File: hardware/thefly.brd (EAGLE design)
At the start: 54 x 54 mm, 37 parts, among them IC1 AP7313-1.8, J1 54-00298-HOLES, U1 SGTL5000XNLA3, U2 MAX4466EXK

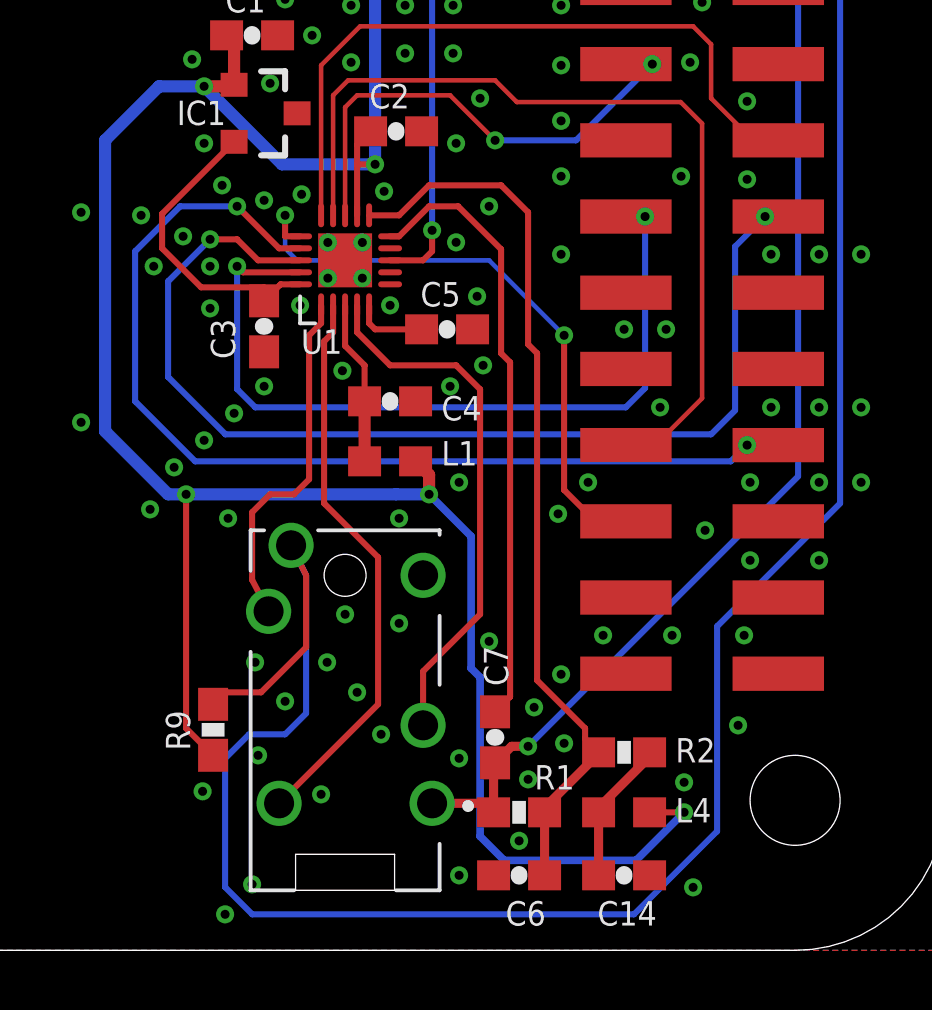
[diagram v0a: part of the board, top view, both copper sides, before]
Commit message: pcb layout changes, removed L4, added comments
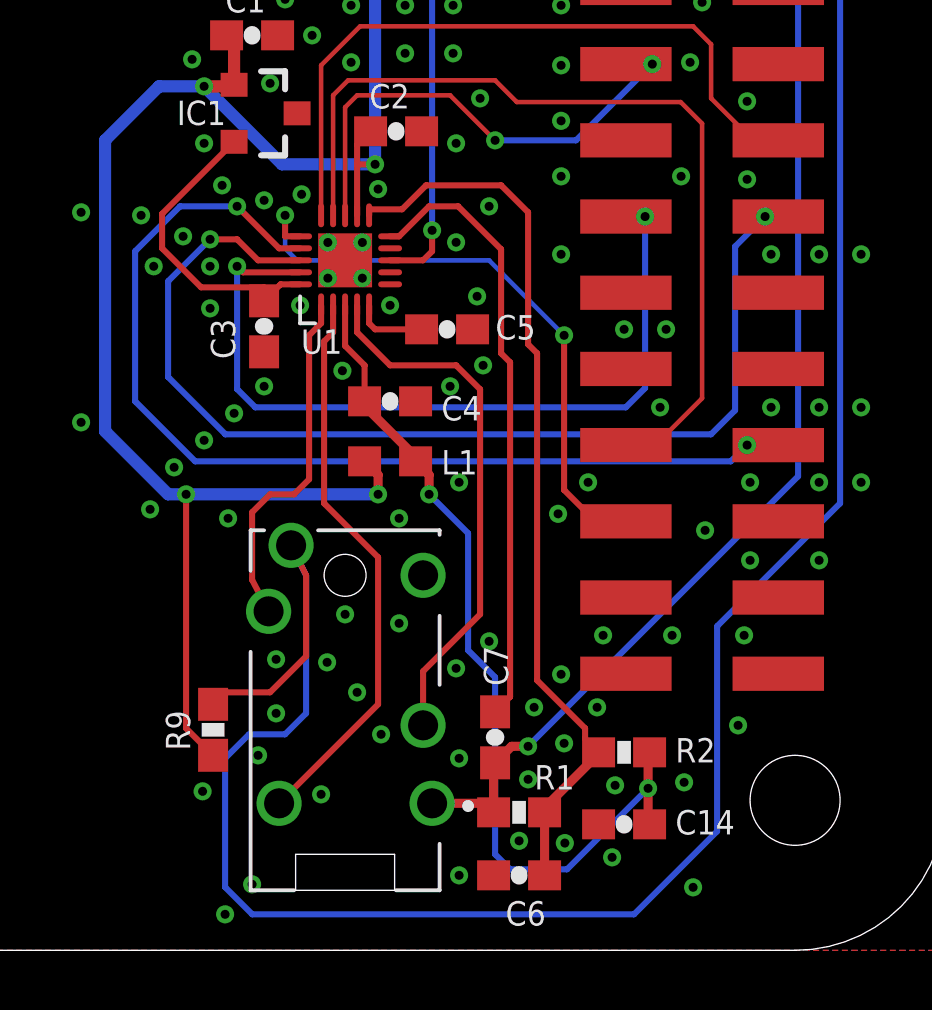
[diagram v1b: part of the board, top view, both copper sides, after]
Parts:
- removed L4: 600, thefly:0603
- moved C14 1.70 mm to (43.3, 4.20), turned to 180 degrees
- turned L1 to 180 degrees
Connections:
- removed net N$1: C14.1, L4.2, R2.1
- net 3.3V: no longer L4.1
- net VDDA: now also C14.1, R2.1
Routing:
- net VDDA: track 5.47 -> 29.4 mm, vias 0 -> 2
- net 3.3V: track 88.5 -> 65.2 mm, vias 6 -> 5
- net N$1: track 4.80 -> 0.00 mm
- net GND: vias 110 -> 115

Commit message: pcb layout use ledc pwm mclk
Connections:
- net MCLK: now also JP1.16; no longer JP1.14
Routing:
- net MCLK: track 16.6 -> 13.7 mm, vias 2 -> 0
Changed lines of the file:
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@@
 <wire x1="34.4" y1="28.5" x2="37.5" y2="28.5" width="0.1524" layer="1"/>
 <wire x1="37.5" y1="28.5" x2="39" y2="27" width="0.1524" layer="1"/>
-<via x="39" y="27" extent="1-16" drill="0.3" shape="octagon"/>
-<wire x1="39" y1="27" x2="41.7" y2="27" width="0.2032" layer="16"/>
-<wire x1="41.7" y1="27" x2="44.24" y2="29.54" width="0.2032" layer="16"/>
-<via x="44.24" y="29.54" extent="1-16" drill="0.3" shape="octagon"/>
-<contactref element="JP1" pad="14"/>
-<wire x1="44.24" y1="29.54" x2="43.36" y2="29.54" width="0.2032" layer="1"/>
+<contactref element="JP1" pad="16"/>
+<wire x1="39" y1="27" x2="39.3" y2="27" width="0.1524" layer="1"/>
+<wire x1="39.3" y1="27" x2="39.6" y2="27" width="0.17" layer="1"/>
+<wire x1="39.6" y1="27" x2="43.36" y2="27" width="0.2" layer="1"/>
 </signal>
 <signal name="VCCA2">

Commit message: layout change to add dc block on mic path
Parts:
- added C15: 100n, thefly:0603-CAP
- moved C14 33.8 mm to (32.8, 36.3), turned to 270 degrees
- moved L3 2.00 mm to (30.0, 33.8)
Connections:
- new net ASDASDASD: C10.2, C14.1, R7.1, U2.4
- net GND: now also C15.2; no longer C14.2
- net MIC2: now also C14.2; no longer C10.2, R7.1, U2.4
- net VDDA: now also C15.1; no longer C14.1
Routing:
- net ASDASDASD: track 0.00 -> 5.31 mm
- net MIC2: track 23.6 -> 19.4 mm
- net GND: vias 115 -> 114
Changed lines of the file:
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@@
 </element>
 <element name="L2" library="thefly" package="0603" value="600" x="35" y="36.2" smashed="yes" rot="R90">
-<attribute name="NAME" x="34.238" y="34.311" size="0.8128" layer="25" font="vector" rot="R90"/>
+<attribute name="NAME" x="34.862" y="34.789" size="0.8128" layer="25" font="vector" rot="R270"/>
 <attribute name="VALUE" x="36.143" y="35.184" size="0.8128" layer="27" font="vector" rot="R90"/>
 </element>
-<element name="L3" library="thefly" package="0603" value="600" x="32" y="33.8" smashed="yes" rot="R90">
-<attribute name="NAME" x="31.238" y="32.911" size="0.8128" layer="25" font="vector" rot="R90"/>
-<attribute name="VALUE" x="33.143" y="32.784" size="0.8128" layer="27" font="vector" rot="R90"/>
+<element name="L3" library="thefly" package="0603" value="600" x="30" y="33.8" smashed="yes" rot="R90">
+<attribute name="NAME" x="29.238" y="32.911" size="0.8128" layer="25" font="vector" rot="R90"/>
+<attribute name="VALUE" x="31.143" y="32.784" size="0.8128" layer="27" font="vector" rot="R90"/>
 </element>
 <element name="R3" library="thefly" package="0603-RES" value="1K" x="38.2" y="44.9" smashed="yes" rot="R180">
@@
 </element>
 <element name="R7" library="thefly" package="0603-RES" value="100K" x="31.9" y="39.7" smashed="yes" rot="R90">
-<attribute name="NAME" x="31.362" y="38.189" size="0.8128" layer="25" font="vector" rot="R270"/>
+<attribute name="NAME" x="30.762" y="38.689" size="0.8128" layer="25" font="vector" rot="R270"/>
 <attribute name="VALUE" x="33.043" y="38.684" size="0.8128" layer="27" font="vector" rot="R90"/>
 </element>
@@
 <attribute name="VALUE" x="30.143" y="46.384" size="0.4064" layer="27" font="vector" rot="R90"/>
 </element>
-<element name="C14" library="thefly" package="0603-CAP" value="100n" x="43.3" y="4.2" smashed="yes" rot="R180">
+<element name="C15" library="thefly" package="0603-CAP" value="100n" x="43.3" y="4.2" smashed="yes" rot="R180">
 <attribute name="NAME" x="45.011" y="3.862" size="0.8128" layer="25" font="vector"/>
 <attribute name="VALUE" x="44.316" y="5.343" size="0.4064" layer="27" font="vector" rot="R180"/>
 </element>
 <element name="U$5" library="thefly" package="THE-FLY-LOGO" value="THE-FLY-LOGO" x="18" y="51"/>
+<element name="C14" library="thefly" package="0603-CAP" value="100n" x="32.8" y="36.3" smashed="yes" rot="R270">
+<attribute name="NAME" x="32.362" y="34.789" size="0.8128" layer="25" font="vector" rot="R270"/>
+<attribute name="VALUE" x="31.657" y="37.316" size="0.4064" layer="27" font="vector" rot="R270"/>
+</element>
 </elements>
 <signals>
@@
 <wire x1="34.65" y1="19.5" x2="34.65" y2="18.3" width="0.2032" layer="1"/>
 <contactref element="R2" pad="1"/>
-<contactref element="C14" pad="1"/>
+<contactref element="C15" pad="1"/>
 <wire x1="44.15" y1="6.45" x2="44.15" y2="6.6" width="0.3048" layer="1"/>
 <via x="36.8" y="15.2" extent="1-16" drill="0.3" shape="octagon"/>
@@
 <via x="51.2" y="41" extent="1-16" drill="0.3" shape="octagon"/>
 <via x="51.2" y="38.4" extent="1-16" drill="0.3" shape="octagon"/>
-<contactref element="C14" pad="2"/>
+<contactref element="C15" pad="2"/>
 <via x="45.6" y="2.1" extent="1-16" drill="0.3" shape="octagon"/>
 <via x="45.3" y="5.6" extent="1-16" drill="0.3" shape="octagon"/>
@@
 <via x="31.1" y="6.5" extent="1-16" drill="0.3" shape="octagon"/>
 <via x="37.8" y="6.4" extent="1-16" drill="0.3" shape="octagon"/>
-<via x="34.4" y="8.6" extent="1-16" drill="0.3" shape="octagon"/>
 <via x="35.2" y="7.2" extent="1-16" drill="0.3" shape="octagon"/>
 <via x="33.2" y="5.2" extent="1-16" drill="0.3" shape="octagon"/>
@@
 <wire x1="33.3" y1="20.3" x2="33.3" y2="14.9" width="0.2032" layer="1"/>
 <wire x1="33.3" y1="14.9" x2="35.1" y2="13.1" width="0.2032" layer="1"/>
-<wire x1="35.1" y1="13.1" x2="35.1" y2="8.2" width="0.2032" layer="1"/>
-<wire x1="35.1" y1="8.2" x2="31.8" y2="4.9" width="0.2032" layer="1"/>
+<wire x1="35.1" y1="13.1" x2="35.1" y2="9.6" width="0.2032" layer="1"/>
+<wire x1="35.1" y1="9.6" x2="31.8" y2="6.3" width="0.2032" layer="1"/>
+<wire x1="31.8" y1="6.3" x2="31.8" y2="4.9" width="0.2032" layer="1"/>
 </signal>
 <signal name="HP-SENSE-L">
@@
 </signal>
 <signal name="MIC2">
-<contactref element="U2" pad="4"/>
-<contactref element="R7" pad="1"/>
-<contactref element="C10" pad="2"/>
 <contactref element="U1" pad="8"/>
-<wire x1="33.35" y1="38.74" x2="32.01" y2="38.74" width="0.3048" layer="1"/>
-<wire x1="32.01" y1="38.74" x2="31.9" y2="38.85" width="0.2032" layer="1"/>
-<wire x1="31.9" y1="38.85" x2="29.9" y2="38.85" width="0.3048" layer="1"/>
 <via x="36.9" y="24" extent="1-16" drill="0.3" shape="octagon"/>
 <wire x1="35.5" y1="23" x2="36.6" y2="23" width="0.2032" layer="1"/>
@@
 <wire x1="36.9" y1="24" x2="36.9" y2="34.487690625" width="0.2032" layer="16"/>
 <wire x1="36.9" y1="34.487690625" x2="36.487690625" y2="34.9" width="0.2032" layer="16"/>
-<wire x1="36.487690625" y1="34.9" x2="33.7" y2="34.9" width="0.2032" layer="16"/>
-<wire x1="33.7" y1="34.9" x2="33.3" y2="35.3" width="0.2032" layer="16"/>
-<wire x1="33.3" y1="35.3" x2="33.3" y2="37.3" width="0.2032" layer="16"/>
-<via x="33.3" y="37.3" extent="1-16" drill="0.3" shape="octagon"/>
-<wire x1="33.3" y1="37.3" x2="33.3" y2="38.74" width="0.3048" layer="1"/>
-<wire x1="33.3" y1="38.74" x2="33.35" y2="38.74" width="0.2032" layer="1"/>
+<wire x1="36.487690625" y1="34.9" x2="31.7" y2="34.9" width="0.2032" layer="16"/>
+<contactref element="C14" pad="2"/>
+<via x="31.7" y="34.9" extent="1-16" drill="0.3" shape="octagon"/>
+<wire x1="31.7" y1="34.9" x2="32.25" y2="34.9" width="0.2032" layer="1"/>
+<wire x1="32.25" y1="34.9" x2="32.8" y2="35.45" width="0.2032" layer="1"/>
 </signal>
 <signal name="N$6">
@@
 <via x="34" y="41.9" extent="1-16" drill="0.3" shape="octagon"/>
 <via x="33.95" y="36.7" extent="1-16" drill="0.3" shape="octagon"/>
-<via x="34" y="37.9" extent="1-16" drill="0.3" shape="octagon"/>
-<via x="32.4" y="37.7" extent="1-16" drill="0.3" shape="octagon"/>
+<via x="33.975" y="37.9" extent="1-16" drill="0.3" shape="octagon"/>
 <via x="32.7" y="43.6" extent="1-16" drill="0.3" shape="octagon"/>
 <via x="30.9" y="45.7" extent="1-16" drill="0.3" shape="octagon"/>
@@
 <via x="30.9" y="41.5" extent="1-16" drill="0.3" shape="octagon"/>
 <via x="32.7" y="41.6" extent="1-16" drill="0.3" shape="octagon"/>
-<via x="32" y="35.9" extent="1-16" drill="0.3" shape="octagon"/>
-<via x="30.8" y="34.7" extent="1-16" drill="0.3" shape="octagon"/>
 <via x="28.3" y="34.4" extent="1-16" drill="0.3" shape="octagon"/>
 <via x="28.3" y="53.4" extent="1-16" drill="0.3" shape="octagon"/>
@@
 <via x="36.1" y="47.8" extent="1-16" drill="0.3" shape="octagon"/>
 <via x="34.2" y="46" extent="1-16" drill="0.3" shape="octagon"/>
+<via x="31.1" y="34.3" extent="1-16" drill="0.3" shape="octagon"/>
+<via x="31.7" y="35.8" extent="1-16" drill="0.3" shape="octagon"/>
+<via x="31.7" y="37.7" extent="1-16" drill="0.3" shape="octagon"/>
 </signal>
 <signal name="N$9">
@@
 <wire x1="34" y1="47" x2="39.05" y2="47" width="0.3048" layer="16"/>
 </signal>
+<signal name="ASDASDASD">
+<contactref element="U2" pad="4"/>
+<contactref element="R7" pad="1"/>
+<contactref element="C10" pad="2"/>
+<contactref element="C14" pad="1"/>
+<wire x1="33.35" y1="38.74" x2="32.01" y2="38.74" width="0.3048" layer="1"/>
+<wire x1="32.01" y1="38.74" x2="31.9" y2="38.85" width="0.2032" layer="1"/>
+<wire x1="31.9" y1="38.85" x2="29.9" y2="38.85" width="0.3048" layer="1"/>
+<wire x1="32.8" y1="37.15" x2="33.35" y2="37.7" width="0.2032" layer="1"/>
+<wire x1="33.35" y1="37.7" x2="33.35" y2="38.74" width="0.2032" layer="1"/>
+</signal>
 </signals>

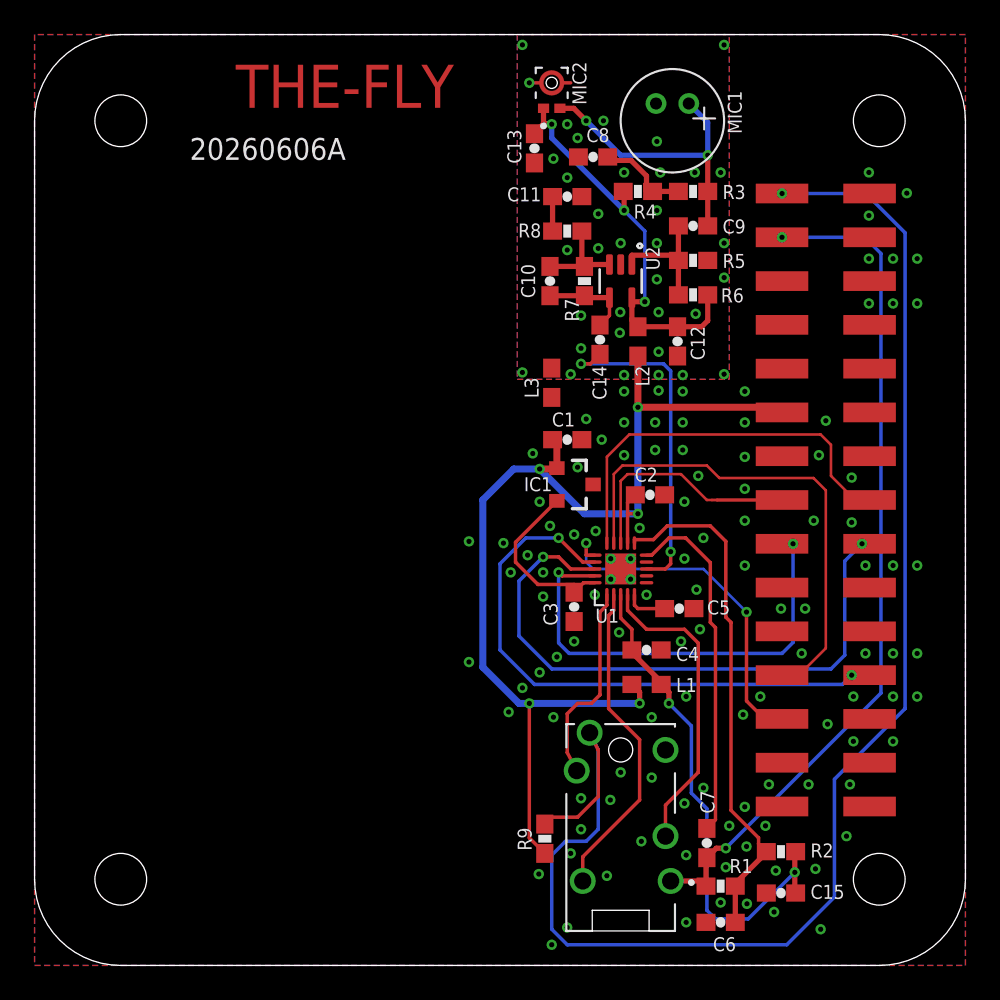
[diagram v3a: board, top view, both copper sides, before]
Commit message: pcb layout removed agnd, more caps
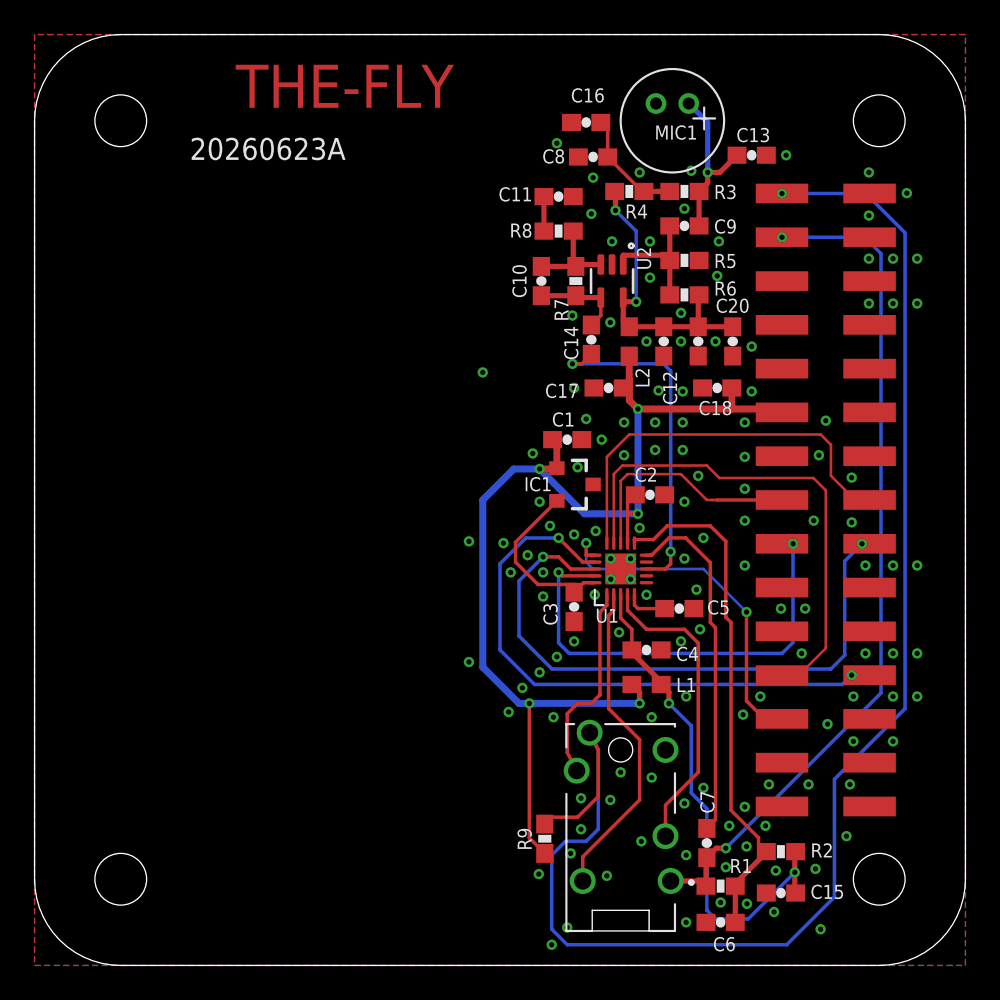
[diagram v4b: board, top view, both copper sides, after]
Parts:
- removed L3: 600, thefly:0603
- removed MIC2: 3SM122KZB1VD-002-R, thefly:MIC_3SM122KZB1VD-002-R
- added C16, C17, C19: 1u, thefly:0603-CAP
- added C18, C20: 10u, thefly:0603-CAP
- C13: value 100n -> 10n
- moved C13 12.6 mm to (41.6, 47.0), turned to 0 degrees
- moved C12 0.80 mm to (36.5, 36.2)
- moved C10 0.50 mm to (29.4, 39.7)
- moved C11 0.50 mm to (30.4, 44.6)
- moved C14 0.50 mm to (32.3, 36.3)
- moved C9 0.50 mm to (37.7, 42.9)
- moved L2 0.50 mm to (34.5, 36.2)
- moved R3 0.50 mm to (37.7, 44.9)
- moved R4 0.50 mm to (34.5, 44.9)
- moved R5 0.50 mm to (37.7, 40.9)
- moved R6 0.50 mm to (37.7, 38.9)
- moved R7 0.50 mm to (31.4, 39.7)
- moved R8 0.50 mm to (30.4, 42.6)
- moved U2 0.50 mm to (33.5, 39.7)
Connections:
- removed net AGND: C11.1, C12.2, C13.1, C8.2, L3.2, MIC1.N, MIC2.3_1, MIC2.3_2, R5.1, U2.2
- net 3.3V: now also C17.1, C18.1
- net GND: now also C11.1, C12.2, C13.2, C16.1, C17.2, C18.2, C19.2, C20.2, C8.2, MIC1.N, R5.1, U2.2; no longer L3.1
- net MICRAW: now also C13.1; no longer MIC2.2
- net N$11: now also C16.2
- net VCCA2: now also C19.1, C20.1; no longer C13.2, MIC2.1
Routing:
- net MICRAW: track 17.3 -> 9.88 mm, vias 2 -> 1
- net VCCA2: track 24.9 -> 17.7 mm, vias 3 -> 2
- net 3.3V: track 65.2 -> 66.8 mm
- net N$11: track 5.42 -> 6.59 mm
- net AGND: track 1.01 -> 0.00 mm, vias 35 -> 0
- net MIC2: track 19.4 -> 19.9 mm
- net GND: vias 114 -> 134
- removed copper zone on layer 1, net AGND
- removed copper zone on layer 16, net AGND
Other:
- board text added: "20260623A"
- board text removed: "20260606A"

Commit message: pcb layout change
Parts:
- moved C19 5.20 mm to (33.3, 36.2)
- moved C14 2.10 mm to (30.2, 36.2)
- moved C20 1.20 mm to (39.3, 36.2)
- moved R7 0.82 mm to (32.2, 39.9)
- moved C10 0.82 mm to (30.2, 39.9)
- moved U2 0.82 mm to (34.3, 39.9)
- moved C11 0.80 mm to (31.2, 44.6)
- moved R8 0.80 mm to (31.2, 42.6)
- moved C12 0.80 mm to (37.3, 36.2)
- moved C9 0.80 mm to (38.5, 42.9)
- moved L2 0.80 mm to (35.3, 36.2)
- moved R3 0.80 mm to (38.5, 44.9)
- moved R4 0.80 mm to (35.3, 44.9)
- moved R5 0.80 mm to (38.5, 40.9)
- moved R6 0.80 mm to (38.5, 38.9)
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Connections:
- net MIC2: now also U1.9
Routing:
- net MIC2: track 19.9 -> 20.9 mm
- net N$11: track 6.59 -> 7.42 mm
- net VCCA2: track 17.7 -> 18.4 mm
- net GND: vias 134 -> 136
